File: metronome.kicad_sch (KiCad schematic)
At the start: 5 parts, among them Q4 2N3904, Q6 2N3906

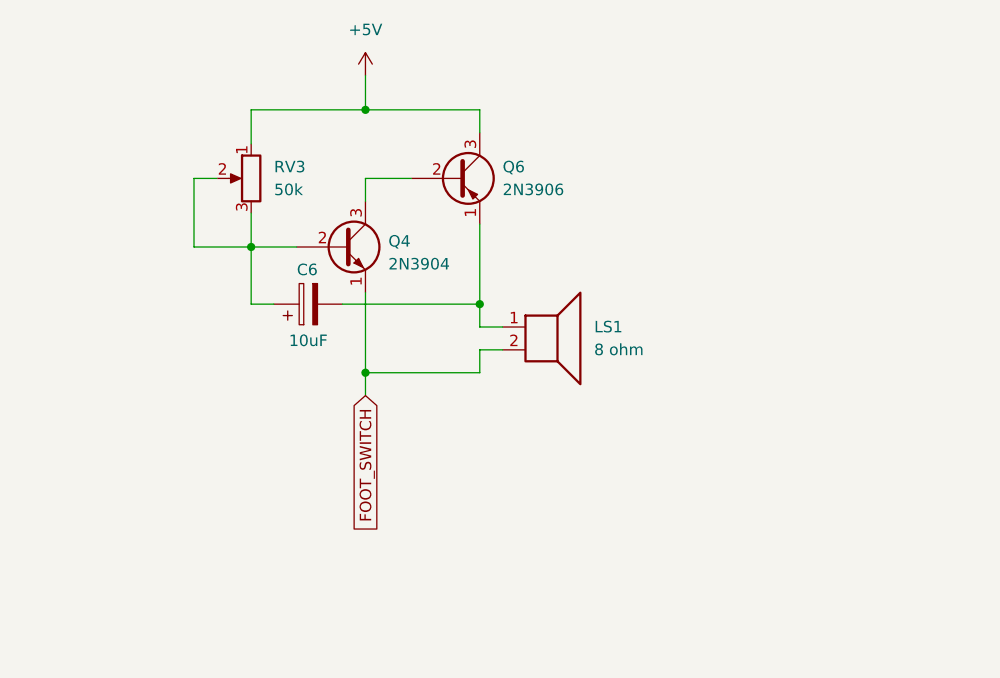
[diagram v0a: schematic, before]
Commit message: Adding metronome commanded by foot switch
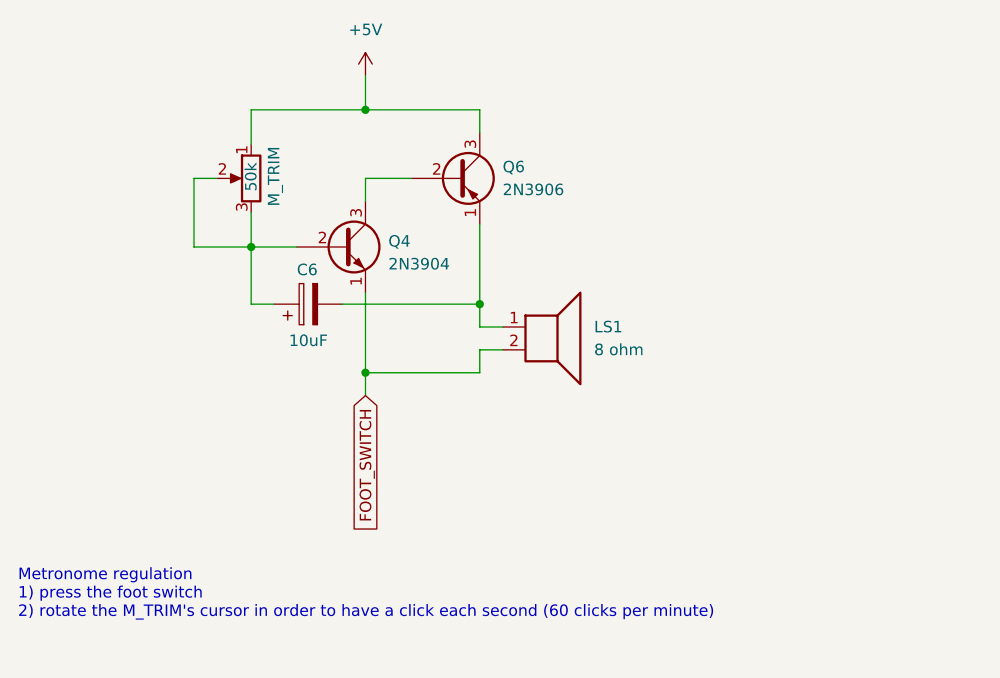
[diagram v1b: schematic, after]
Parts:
- renumbered RV3 to M_TRIM
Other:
- note added: "Metronome regulation 1) press the foot switch 2) rotate the M_TRIM's cursor in order to have a click each second (60 clicks per minute)"
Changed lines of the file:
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@@
+		)
+	)
+	(text "Metronome regulation\n1) press the foot switch\n2) rotate the M_TRIM's cursor in order to have a click each second (60 clicks per minute)"
+		(exclude_from_sim no)
+		(at 121.412 131.318 0)
+		(effects
+			(font
+				(size 1.27 1.27)
+			)
+			(justify left)
 		)
 	)
@@
 		(on_board yes)
 		(dnp no)
-		(property "Reference" "RV3"
-			(at 149.86 83.8199 0)
+		(property "Reference" "M_TRIM"
+			(at 149.86 81.534 90)
 			(effects
 				(font
@@
 		)
 		(property "Value" "50k"
-			(at 149.86 86.3599 0)
+			(at 147.32 83.312 90)
 			(effects
 				(font
@@
 			(project ""
 				(path "/443fc4b5-0df2-45f7-86a3-68fb41149ce4/c56b1fe6-b240-47cd-9e98-b7dea85fd84b"
-					(reference "RV3")
+					(reference "M_TRIM")
 					(unit 1)
 				)

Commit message: Fix metronome R and C values to allow frequency down to 1 Hz
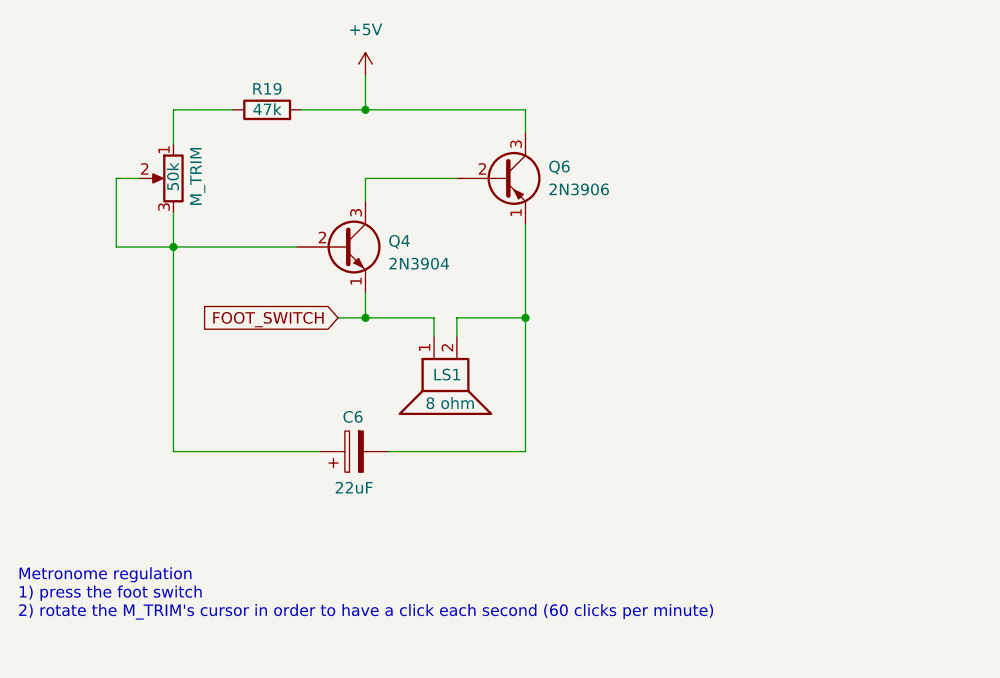
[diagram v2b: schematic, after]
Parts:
- added R19: 47k, symbol Device:R
- C6: value 10uF -> 22uF
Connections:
- net +5V: now also R19.2; no longer M_TRIM.1
- net FOOT_SWITCH: now also LS1.1; no longer LS1.2
- net at C6.2, Q6.1 (E): now also LS1.2; no longer LS1.1
- new net: M_TRIM.1, R19.1
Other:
- moved on the sheet: C6, LS1, M_TRIM, Q6

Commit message: Show a couple of R values in metronome circuit depending on speaker resistance
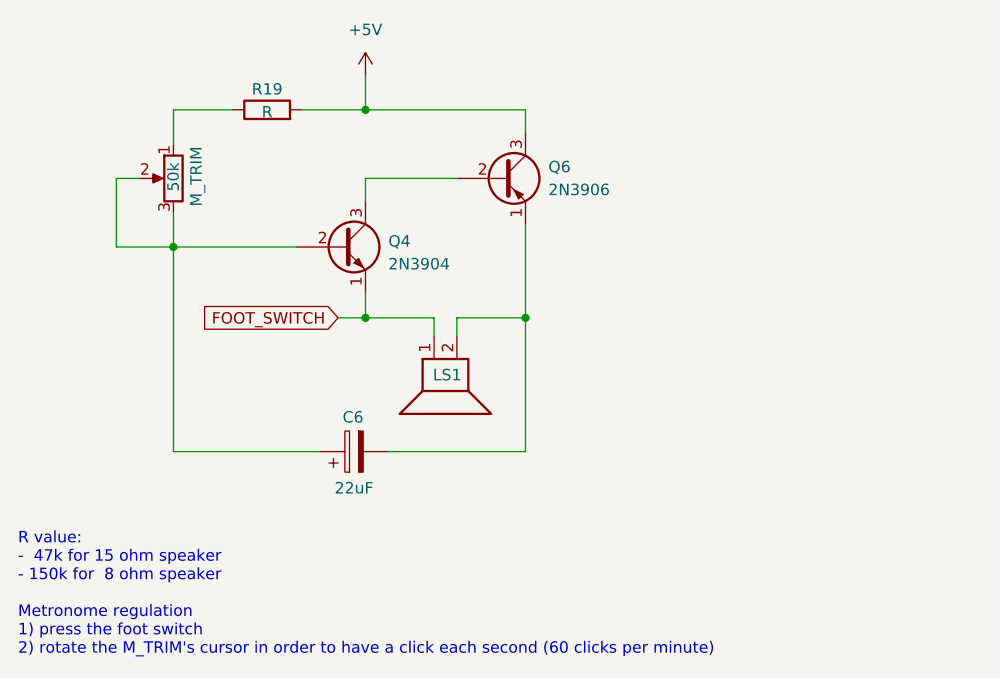
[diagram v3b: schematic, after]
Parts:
- LS1: value 8 ohm -> ~
- R19: value 47k -> R
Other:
- note added: "R value: - 47k for 15 ohm speaker - 150k for 8 ohm speaker Metronome regulation 1) press the foot switch 2) rotate the M_TRIM's cursor in order to have a click each second (60 clicks per minute)"
- note removed: "Metronome regulation 1) press the foot switch 2) rotate the M_TRIM's cursor in order to have a click each second (60 clicks per minute)"
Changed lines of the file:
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@@
 		)
 	)
-	(text "Metronome regulation\n1) press the foot switch\n2) rotate the M_TRIM's cursor in order to have a click each second (60 clicks per minute)"
+	(text "R value:\n-  47k for 15 ohm speaker\n- 150k for  8 ohm speaker\n\nMetronome regulation\n1) press the foot switch\n2) rotate the M_TRIM's cursor in order to have a click each second (60 clicks per minute)"
 		(exclude_from_sim no)
 		(at 121.412 131.318 0)
@@
 			)
 		)
-		(property "Value" "47k"
-			(at 149.098 77.47 90)
+		(property "Value" "R"
+			(at 149.098 77.724 90)
 			(effects
 				(font
@@
 			)
 		)
-		(property "Value" "8 ohm"
+		(property "Value" "~"
 			(at 172.212 110.109 90)
 			(effects
